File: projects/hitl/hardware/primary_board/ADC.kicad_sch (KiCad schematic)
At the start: 30 parts, among them J16 CONN_01X03, J17 CONN_01X03, J18 CONN_01X03, J19 CONN_01X03, U6 AD7091R-5BRUZ, U7 MCP6001, U8 74HCT4051D

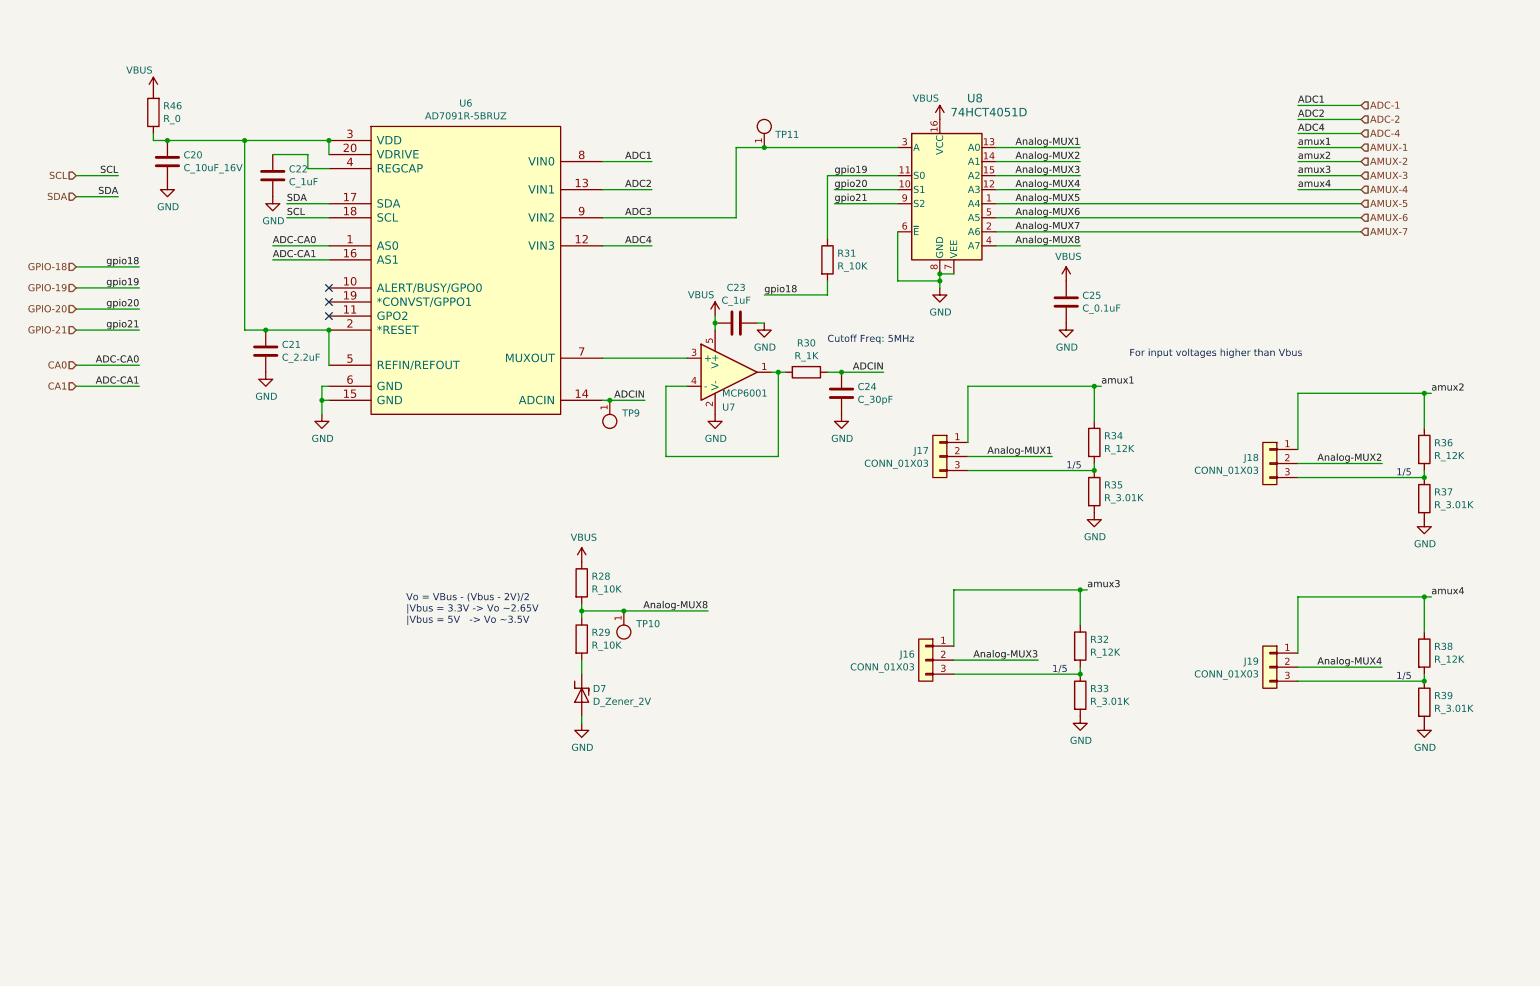
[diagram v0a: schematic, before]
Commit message: Split schematic into sheets
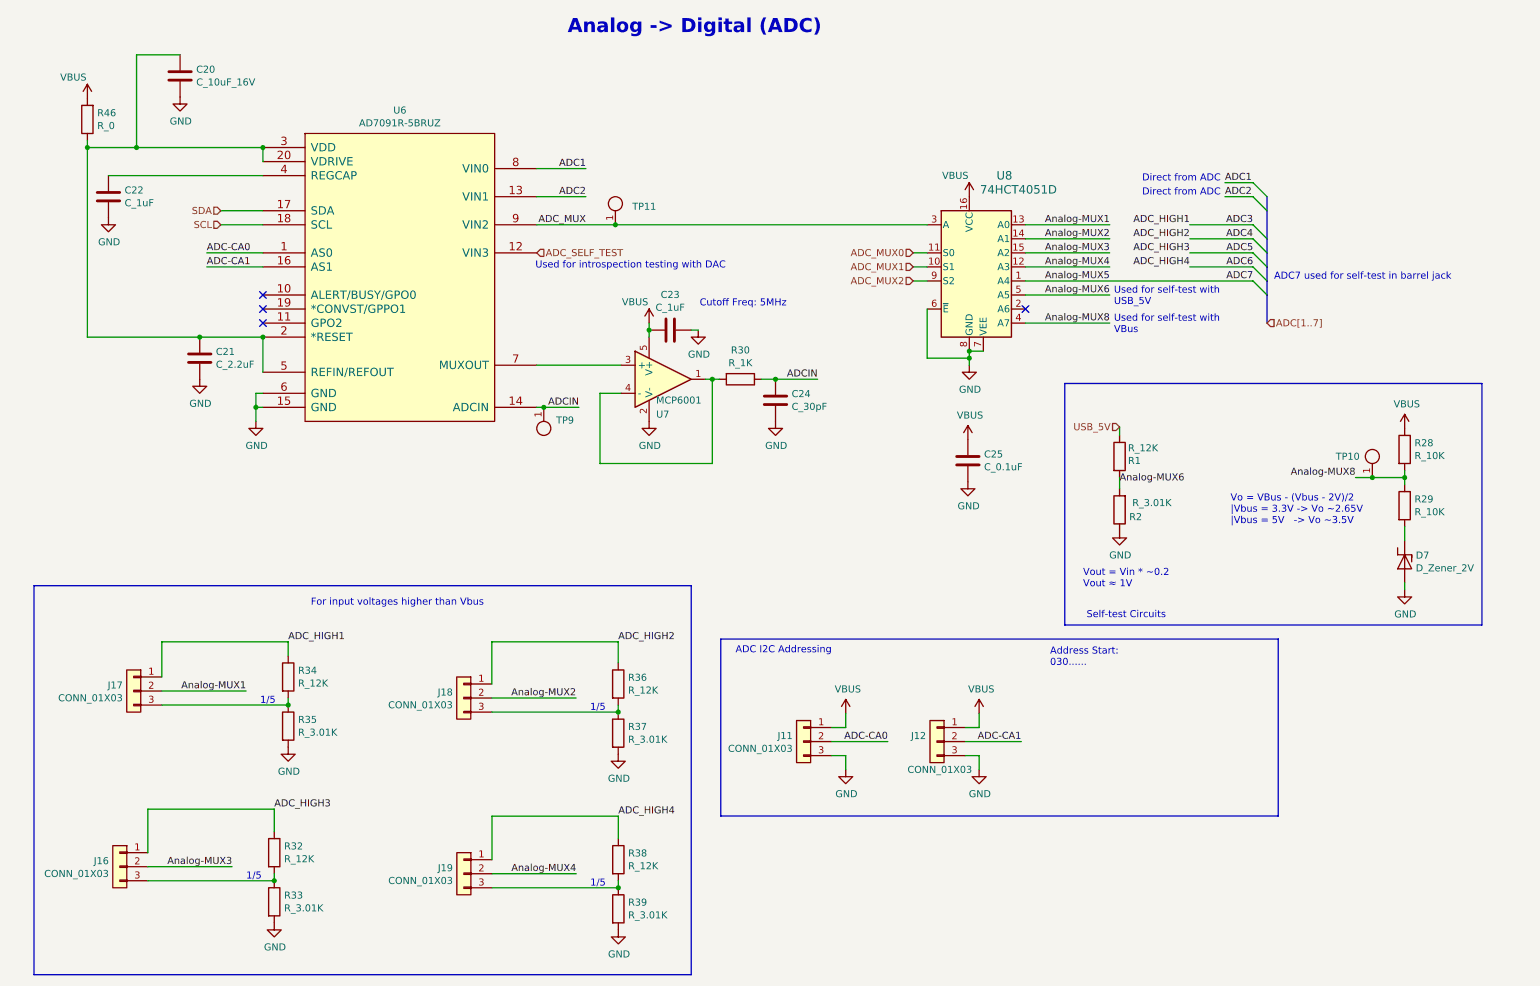
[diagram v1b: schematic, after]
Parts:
- removed R31: R_10K, footprints:R_0805_OEM, symbol formula:R_10K
- added J11, J12: CONN_01X03, footprints:PinHeader_1x03_P2.54mm_Vertical, symbol formula:CONN_01X03
- added R1: R_12K, footprints:R_0805_OEM, symbol formula:R_12K
- added R2: R_3.01K, footprints:R_0805_OEM, symbol formula:R_3.01K
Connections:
- net AMUX-1 is gone; now on net ADC3: J17.1 (P1), R34.1
- net ADC3: no longer TP11.1, U6.9 (VIN2), U8.3 (A)
- net GND: now also J11.3 (P3), J12.3 (P3), R2.1
- net VBUS: now also J11.1 (P1), J12.1 (P1)
- net ADC-1 renamed ADC1
- net ADC-2 renamed ADC2
- net ADC-4 renamed ADC_SELF_TEST
- net AMUX-2 renamed ADC4
- net AMUX-3 renamed ADC5
- net AMUX-4 renamed ADC6
- net AMUX-5 renamed ADC7
- net AMUX-6 renamed Analog-MUX6
- net Analog-MUX6: now also R1.2, R2.2
- net AMUX-7: no longer names the net of U8.2 (A6)
- net CA0 renamed ADC-CA0
- net ADC-CA0: now also J11.2 (P2)
- net CA1 renamed ADC-CA1
- net ADC-CA1: now also J12.2 (P2)
- net GPIO-19 renamed ADC_MUX0
- net GPIO-20 renamed ADC_MUX1
- net GPIO-21 renamed ADC_MUX2
- new net ADC_MUX: TP11.1, U6.9 (VIN2), U8.3 (A)
- new net USB_5V: R1.1
- no-connect marks 3 -> 4
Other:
- note added: "ADC I2C Addressing"
- note added: "ADC7 used for self-test in barrel jack"
- note added: "Address Start: 030......"
- note added: "Analog -> Digital (ADC)"
- note added: "Direct from ADC"
- note added: "Self-test Circuits"
- note added: "Used for introspection testing with DAC"
- note added: "Used for self-test with USB_5V"
- note added: "Used for self-test with VBus"
- note added: "Vout = Vin * ~0.2 Vout ≈ 1V"
- moved on the sheet: C20, C21, C22, C23, C24, C25, D7, J16, J17, J18, J19, R28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
